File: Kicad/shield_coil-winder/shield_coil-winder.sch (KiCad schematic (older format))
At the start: 32 parts, among them K1 SOCKET_DRIVER_B, K2 SOCKET_DRIVER_A, P1 Power, P10 MicroSteps, P11 MOTOR-B, P12 MOTOR-A, P13 ALIM_EXT, P2 Analog, P3 Digital, P4 Digital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

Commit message: PCB v1.0
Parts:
- C1, C2, C3: footprint (none) -> mod:C_Horiz_15.5x6.5
- C4: footprint (none) -> Capacitors_ThroughHole:C_Disc_D3_P2.5
- D1: footprint (none) -> LEDs:LED-3MM
- D2, D3: footprint (none) -> Diodes_ThroughHole:Diode_DO-41_SOD81_Horizontal_RM10
- F1: footprint (none) -> Varistors:RV_Disc_D7_W3.4_P5
- K1, K2: footprint (none) -> mod:Driver_Socket
- P10, P9: footprint (none) -> Pin_Headers:Pin_Header_Straight_2x03
- P11, P12: footprint Sockets_MOLEX_KK-System:Socket_MOLEX-KK-RM2-54mm_Lock_4pin_straight -> Pin_Headers:Pin_Header_Straight_1x04
- P13: footprint Sockets_MOLEX_KK-System:Socket_MOLEX-KK-RM2-54mm_Lock_2pin_straight -> Connect:bornier2
- R1, R3: footprint Resistors_SMD:R_0603 -> Resistors_ThroughHole:Resistor_Horizontal_RM10mm
- R2, R4, R5: footprint (none) -> Resistors_ThroughHole:Resistor_Horizontal_RM10mm
- SW1: footprint (none) -> mod:Rotary_encoder-ALPS
- SW2: footprint (none) -> Buttons_Switches_ThroughHole:SW_PUSH_6mm
- U1: footprint (none) -> mod:PCF8574_Board
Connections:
- net A4(SDA): no longer P2.5 (P5)
- net A5(SCL): no longer P2.6 (P6)
- net 10(**/SS) renamed DIR-B_10
- net DIR-B_10: now also K1.8 (DIR)
- net 13(SCK) renamed LED_13(SCK)
- net 2 renamed IT_2
- net 3(**) renamed IT_3
- net 4 renamed EN-A_5
- net EN-A_5: now also P4.3 (P3); no longer P4.4 (P4), SW1.4
- net 5(**) renamed STEP-A_6
- net STEP-A_6: now also P4.2 (P2); no longer P4.3 (P3)
- net 6(**) renamed DIR-A_7
- net DIR-A_7: now also P4.1 (P1); no longer P4.2 (P2)
- net 7 renamed EN-B_8
- net EN-B_8: now also P3.10 (P10); no longer P4.1 (P1)
- net 8 renamed STEP-B_9
- net STEP-B_9: now also P3.9 (P9); no longer P3.10 (P10)
- removed net 9(**): K1.8 (DIR), P3.9 (P9)
- new net A4: P2.5 (P5)
- new net A5: P2.6 (P6)
- new net SW-ENC_4: P4.4 (P4), SW1.4
- no-connect marks 14 -> 18

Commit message: V1.1 pcb
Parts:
- removed F1: 3A, Varistors:RV_Disc_D7_W3.4_P5, symbol FUSE
- added D4: LED, LEDs:LED-3MM, symbol LED
- added F1: MF-R050, Varistors:RV_Disc_D7_W3.4_P5, symbol F_Small
- added R6: 10K, Resistors_ThroughHole:Resistor_Horizontal_RM10mm, symbol R
- K1: value SOCKET_DRIVER_B -> SOCKET_DRIVER_A
- K2: value SOCKET_DRIVER_A -> SOCKET_DRIVER_B
- P11: value MOTOR-B -> MOTOR-A
- P12: value MOTOR-A -> MOTOR-B
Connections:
- net GND: now also P5.1 (P1), P6.1 (P1), P7.1 (P1), P8.1 (P1), R6.1
- net VCC: now also D4.2 (A), F1.2
- net at P13.1 (P1): now also F1.1
- new net: D4.1 (K), R6.2
- no-connect marks 18 -> 14
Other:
- moved on the sheet: C3, C4, D2, D3, SW1, SW2

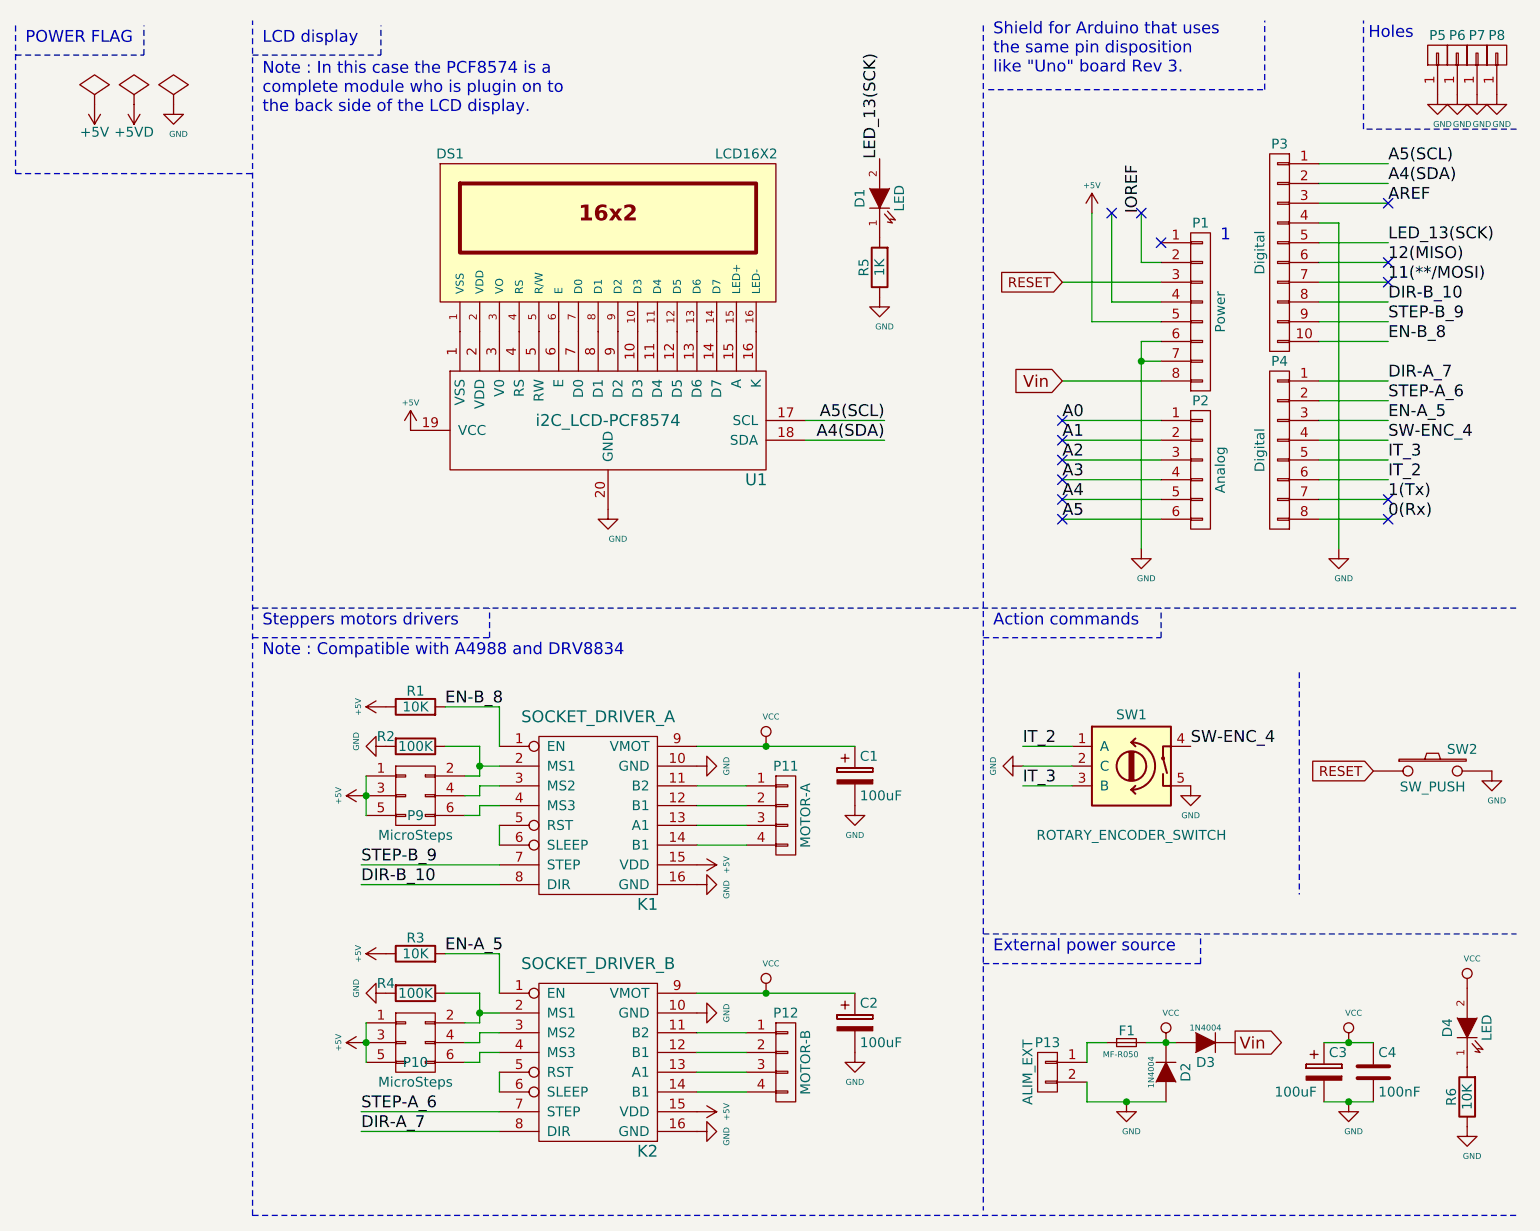
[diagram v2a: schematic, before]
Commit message: Correction label pin on sockets
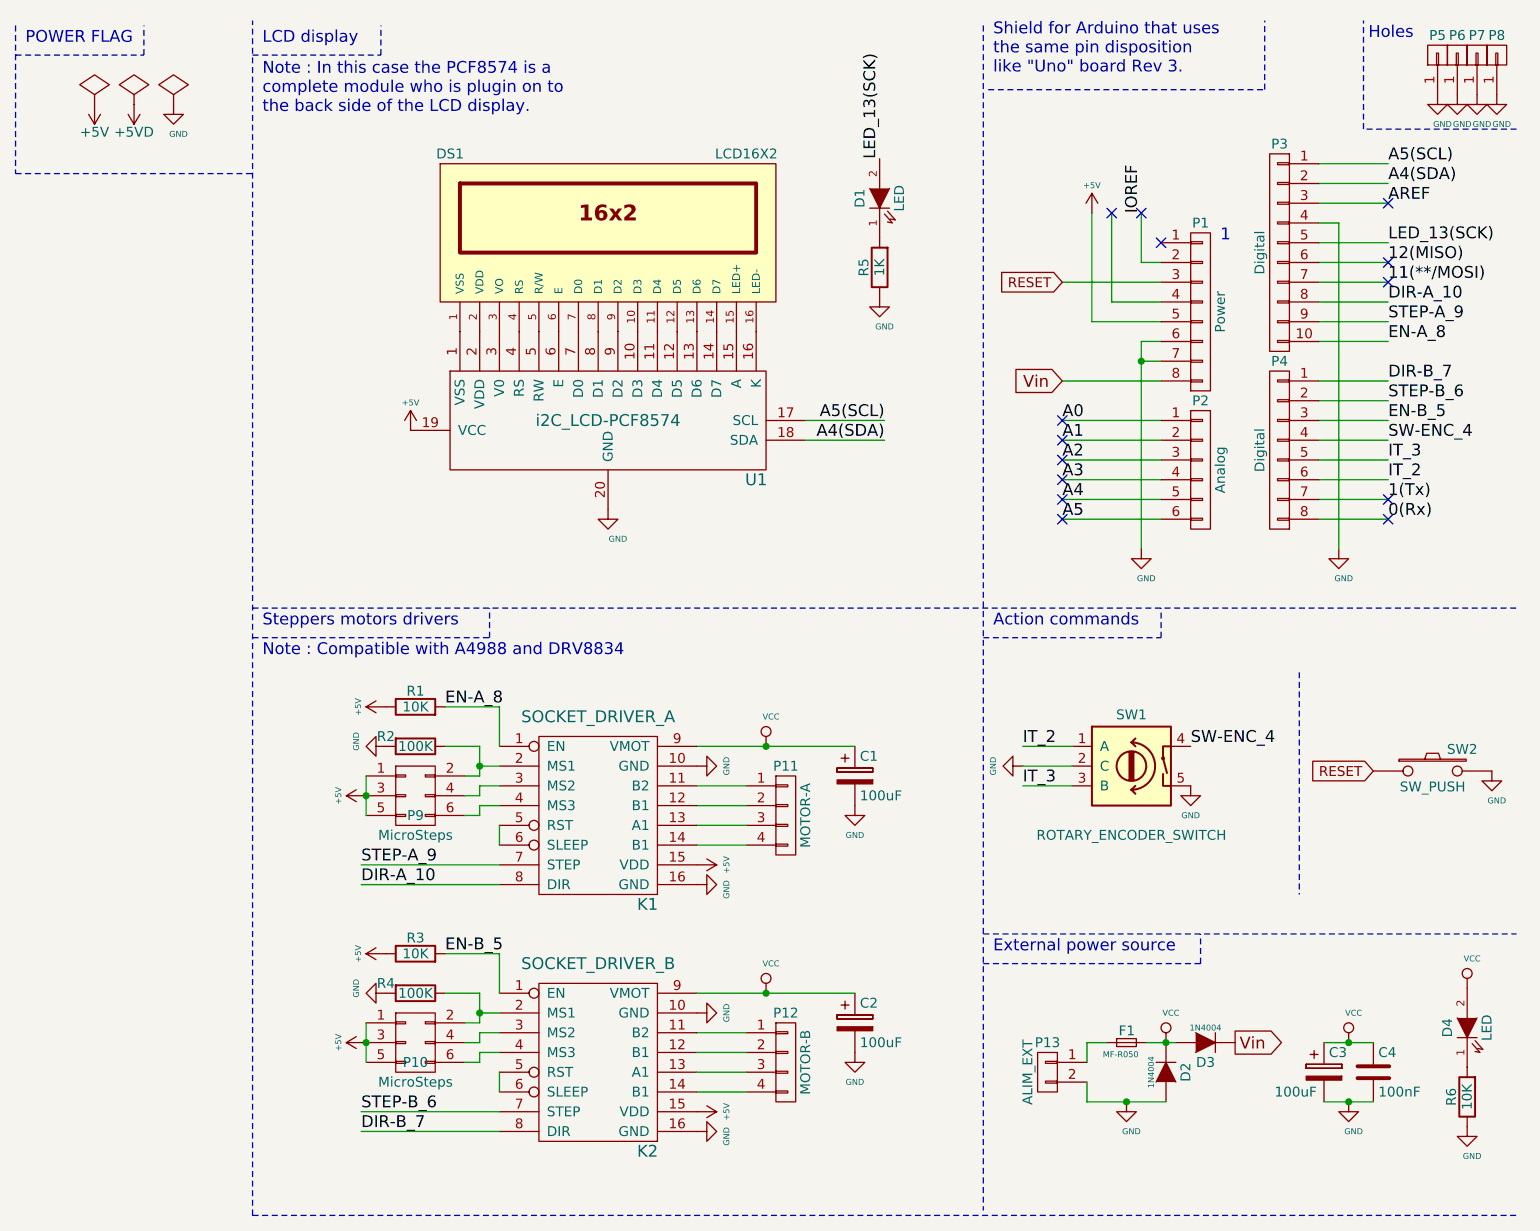
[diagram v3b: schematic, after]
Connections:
- net DIR-A_7 renamed DIR-B_7
- net DIR-B_10 renamed DIR-A_10
- net EN-A_5 renamed EN-B_5
- net EN-B_8 renamed EN-A_8
- net STEP-A_6 renamed STEP-B_6
- net STEP-B_9 renamed STEP-A_9
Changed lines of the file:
@@
 IT_3
 Text Label 10550 2100 0    60   ~ 0
-EN-B_8
+EN-A_8
 Text Label 10550 1800 0    60   ~ 0
 11(**/MOSI)
@@
 $EndComp
 Text Label 5350 6000 0    60   ~ 0
-STEP-A_6
+STEP-B_6
 Text Label 5350 6100 0    60   ~ 0
-DIR-A_7
+DIR-B_7
 Text Label 10550 1900 0    60   ~ 0
-DIR-B_10
+DIR-A_10
 $Comp
 L CONN_01X02 P13
@@
 	9400 1800 8900 1800
 Text Label 5775 5200 0    60   ~ 0
-EN-A_5
+EN-B_5
 Text Label 10550 1200 0    60   ~ 0
 A5(SCL)
@@
 A4(SDA)
 Text Label 5775 3950 0    60   ~ 0
-EN-B_8
+EN-A_8
 Wire Wire Line
 	7600 2500 8000 2500
@@
 A5
 Text Label 5350 4750 0    60   ~ 0
-STEP-B_9
+STEP-A_9
 Text Label 10550 2000 0    60   ~ 0
-STEP-B_9
+STEP-A_9
 Text Label 5350 4850 0    60   ~ 0
-DIR-B_10
+DIR-A_10
 Text Label 10550 2400 0    60   ~ 0
-STEP-A_6
+STEP-B_6
 Text Label 10550 2300 0    60   ~ 0
-DIR-A_7
+DIR-B_7
 NoConn ~ 10550 1700
 NoConn ~ 10550 1800
@@
 SW-ENC_4
 Text Label 10550 2500 0    60   ~ 0
-EN-A_5
+EN-B_5
 $Comp
 L VCC #PWR027
